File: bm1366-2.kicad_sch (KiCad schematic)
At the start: 88 parts, among them U1 25MHz, U13 ADP171AUJ-R7, U18 TLV3544, U19 BM1366_mode0, U22 BM1366_mode0, U23 ADP171AUJ-R7

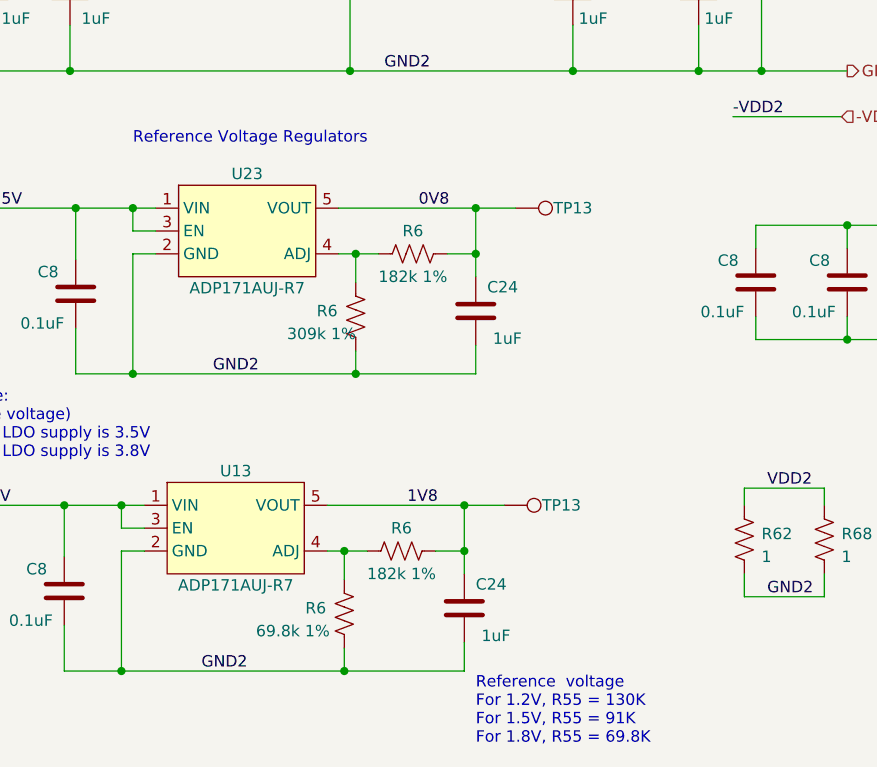
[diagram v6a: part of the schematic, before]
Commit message: switch out reference LDOs for AP7331
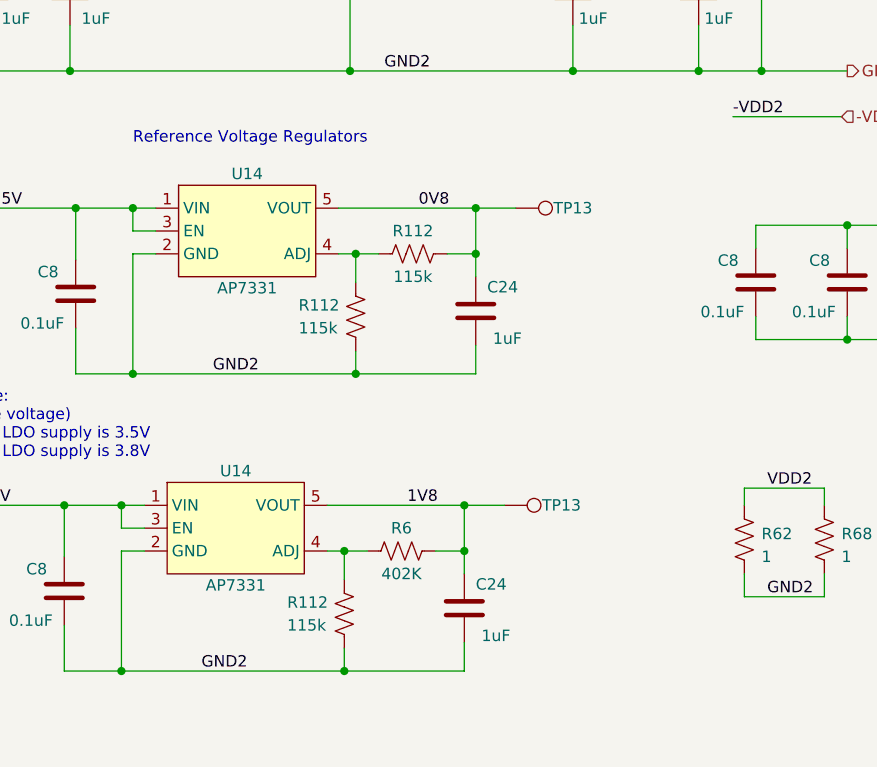
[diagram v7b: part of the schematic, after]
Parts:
- removed R6 (x2): 182k 1%, Resistor_SMD:R_0402_1005Metric, symbol Device:R_US
- removed R6: 69.8k 1%, Resistor_SMD:R_0402_1005Metric, symbol Device:R_US
- removed R6: 309k 1%, Resistor_SMD:R_0402_1005Metric, symbol Device:R_US
- removed U13, U23: ADP171AUJ-R7, Package_TO_SOT_SMD:TSOT-23-5, symbol bitaxe:ADP171AUJ-R7
- added R112 (x3): 115k, Resistor_SMD:R_0402_1005Metric, symbol Device:R_US
- added R6: 402K, Resistor_SMD:R_0402_1005Metric, symbol Device:R_US
- added U14 (x2): AP7331, Package_TO_SOT_SMD:TSOT-23-5, symbol bitaxe:AP7331
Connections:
- net 0V8: now also R112.2, U14.5 (VOUT)
- net 1V8: now also R6.1, U14.5 (VOUT)
- net 5V: now also U14.1 (VIN), U14.1 (VIN), U14.3 (EN), U14.3 (EN)
- net GND2: now also R112.1, R112.1, U14.2 (GND), U14.2 (GND)
- new net: R112.2, R6.2, U14.4 (ADJ)
- new net: R112.1, R112.2, U14.4 (ADJ)
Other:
- note removed: "Reference voltage For 1.2V, R55 = 130K For 1.5V, R55 = 91K For 1.8V, R55 = 69.8K"

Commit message: Fix DK partnumber for 402K resistor
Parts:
- R6: DK YAG3015CT-ND -> YAG3151CT-ND; PARTNO RC0402FR-07182KL -> RC0402FR-07402KL
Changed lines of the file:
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@@
       (effects (font (size 1.27 1.27)) hide)
     )
-    (property "DK" "YAG3015CT-ND" (at 83.185 180.975 0)
+    (property "DK" "YAG3151CT-ND" (at 83.185 180.975 0)
       (effects (font (size 1.27 1.27)) hide)
     )
-    (property "PARTNO" "RC0402FR-07182KL" (at 83.185 180.975 0)
+    (property "PARTNO" "RC0402FR-07402KL" (at 83.185 180.975 0)
       (effects (font (size 1.27 1.27)) hide)
     )
